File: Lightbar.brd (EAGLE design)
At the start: 91.4 x 11.4 mm, 20 parts, among them IC1 PAM2863ECR, IC2 PAM2863ECR

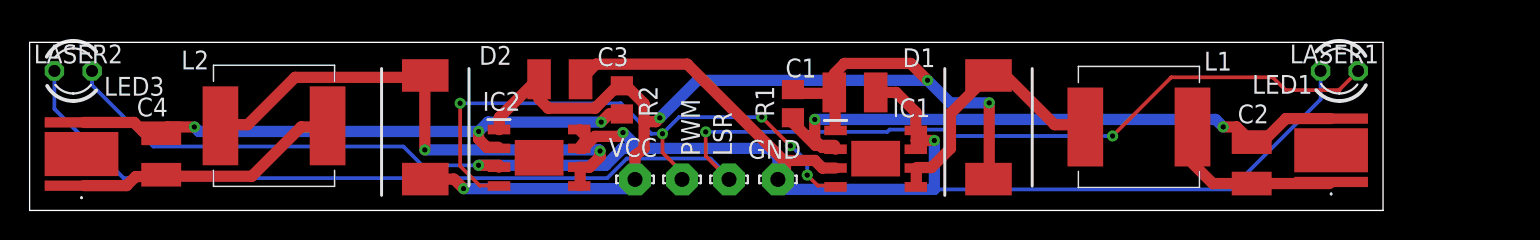
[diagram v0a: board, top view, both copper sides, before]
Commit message: Added notches and screw holes
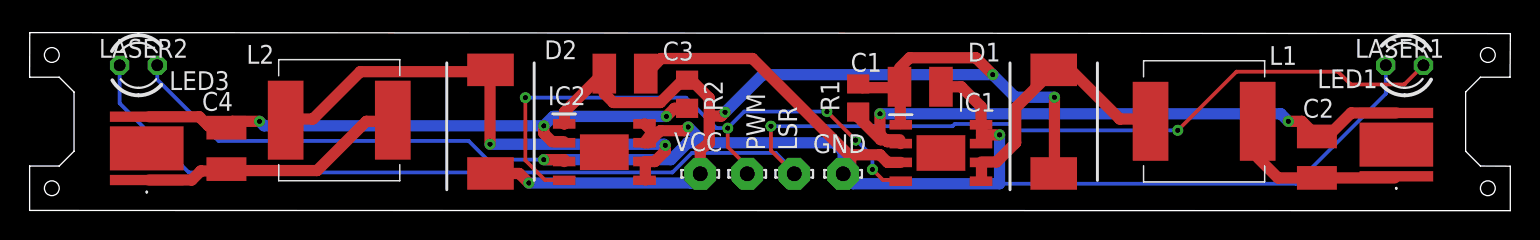
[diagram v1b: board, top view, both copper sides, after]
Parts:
- moved C1 4.42 mm to (60.2, 8.35)
- moved C2 4.42 mm to (87.0, 3.60)
- moved C3 4.42 mm to (40.2, 9.24)
- moved D1 4.42 mm to (69.2, 6.00)
- moved GND 4.42 mm to (55.0, 2.48)
- moved IC1 4.42 mm to (61.6, 3.88)
- moved IC2 4.42 mm to (38.8, 3.94)
- moved LASER1 4.42 mm to (92.9, 9.80)
- moved LED1 4.42 mm to (92.3, 4.45)
- moved LSR 4.42 mm to (51.6, 2.48)
- moved R1 4.42 mm to (56.0, 7.59)
- moved VCC 4.42 mm to (45.3, 2.48)
- moved C4 4.42 mm to (13.3, 4.19)
- moved LASER2 4.42 mm to (7.35, 9.80)
- moved LED3 4.42 mm to (7.91, 4.19)
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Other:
- board size 91.4 x 11.4 mm -> 100 x 12 mm
